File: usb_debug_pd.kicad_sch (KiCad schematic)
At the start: 87 parts, among them J4 Tag-Connect_TC2050-IDC-NL_2x5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, J7 USB-C_Kycon_KUSBX-SL2-CS1N24-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, Q12 DMG1012T-7, Q3 DMG1012T-7, U29 W25Q80DV_USON, U30 TPS65988DHRSHR, U31 NTS0102_XSON, U32 NCP718BSN330T1G, U34 FT230X_QFN, U40 AP22615A_TSOT26, U42 TPD4E05U06QDQARQ1

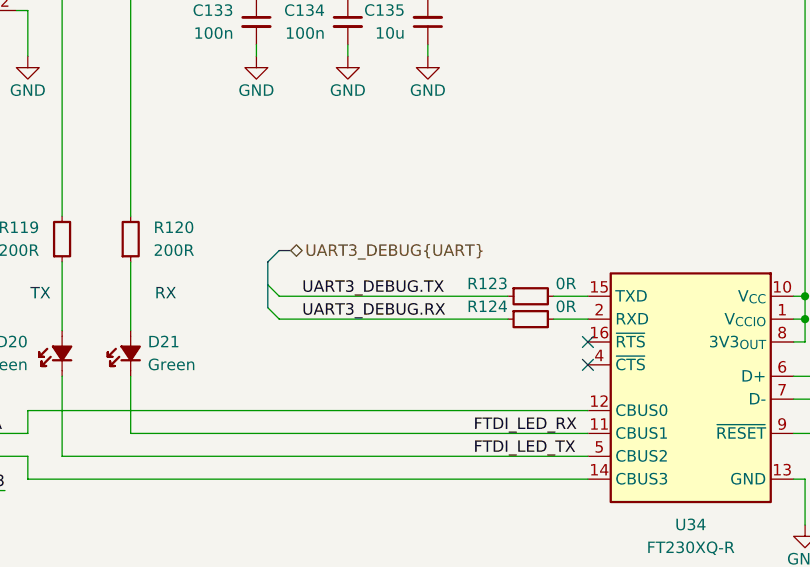
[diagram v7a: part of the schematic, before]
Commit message: [#85326] Update level shifters, fix UART cross
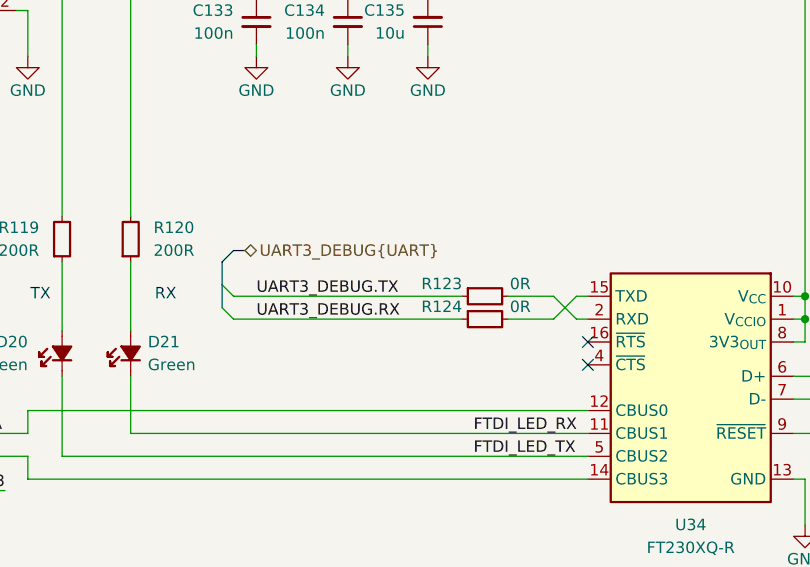
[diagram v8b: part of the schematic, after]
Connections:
- net at R124.2: now also U34.15 (TXD); no longer U34.2 (RXD)
- net at R123.2: now also U34.2 (RXD); no longer U34.15 (TXD)
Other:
- moved on the sheet: R123, R124
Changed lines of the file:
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@@
 	)
 	(bus_entry
-		(at 135.89 100.33)
+		(at 130.81 100.33)
 		(size 1.27 1.27)
 		(stroke
@@
 	)
 	(bus_entry
-		(at 135.89 97.79)
+		(at 130.81 97.79)
 		(size 1.27 1.27)
 		(stroke
@@
 	(wire
 		(pts
+			(xy 162.56 99.06) (xy 167.64 99.06)
+		)
+		(stroke
+			(width 0)
+			(type default)
+		)
+	)
+	(wire
+		(pts
 			(xy 227.33 114.3) (xy 212.09 114.3)
 		)
@@
 	(wire
 		(pts
+			(xy 170.18 101.6) (xy 167.64 99.06)
+		)
+		(stroke
+			(width 0)
+			(type default)
+		)
+	)
+	(wire
+		(pts
 			(xy 330.2 201.93) (xy 328.93 201.93)
 		)
@@
 	(bus
 		(pts
-			(xy 137.16 93.98) (xy 135.89 95.25)
+			(xy 132.08 93.98) (xy 130.81 95.25)
 		)
 		(stroke
@@
 	(wire
 		(pts
-			(xy 171.45 99.06) (xy 167.64 99.06)
-		)
-		(stroke
-			(width 0)
-			(type default)
-		)
-	)
-	(wire
-		(pts
 			(xy 140.97 215.9) (xy 149.86 215.9)
 		)
@@
 	(wire
 		(pts
-			(xy 171.45 101.6) (xy 167.64 101.6)
+			(xy 217.17 257.81) (xy 242.57 257.81)
 		)
 		(stroke
@@
 	(wire
 		(pts
-			(xy 217.17 257.81) (xy 242.57 257.81)
+			(xy 162.56 101.6) (xy 167.64 101.6)
 		)
 		(stroke
@@
 	(wire
 		(pts
+			(xy 170.18 99.06) (xy 171.45 99.06)
+		)
+		(stroke
+			(width 0)
+			(type default)
+		)
+	)
+	(wire
+		(pts
 			(xy 245.11 222.25) (xy 245.11 217.17)
 		)
@@
 		)
 	)
+	(wire
+		(pts
+			(xy 170.18 101.6) (xy 171.45 101.6)
+		)
+		(stroke
+			(width 0)
+			(type default)
+		)
+	)
 	(bus
 		(pts
-			(xy 135.89 95.25) (xy 135.89 97.79)
+			(xy 130.81 95.25) (xy 130.81 97.79)
 		)
 		(stroke
@@
 	(bus
 		(pts
-			(xy 138.43 93.98) (xy 137.16 93.98)
+			(xy 133.35 93.98) (xy 132.08 93.98)
 		)
 		(stroke
@@
 	(bus
 		(pts
-			(xy 135.89 97.79) (xy 135.89 100.33)
+			(xy 130.81 97.79) (xy 130.81 100.33)
 		)
 		(stroke
@@
 	(wire
 		(pts
-			(xy 137.16 101.6) (xy 162.56 101.6)
+			(xy 132.08 101.6) (xy 157.48 101.6)
 		)
 		(stroke
@@
 	(wire
 		(pts
-			(xy 137.16 99.06) (xy 162.56 99.06)
+			(xy 170.18 99.06) (xy 167.64 101.6)
+		)
+		(stroke
+			(width 0)
+			(type default)
+		)
+	)
+	(wire
+		(pts
+			(xy 132.08 99.06) (xy 157.48 99.06)
 		)
 		(stroke
@@
 	)
 	(label "UART3_DEBUG.RX"
-		(at 139.7 101.6 0)
+		(at 134.62 101.6 0)
 		(effects
 			(font
@@
 	)
 	(label "UART3_DEBUG.TX"
-		(at 139.7 99.06 0)
+		(at 134.62 99.06 0)
 		(effects
 			(font
@@
 	(hierarchical_label "UART3_DEBUG{UART}"
 		(shape bidirectional)
-		(at 138.43 93.98 0)
+		(at 133.35 93.98 0)
 		(effects
 			(font
@@
 	(symbol
 		(lib_id "antmicroResistors0402:R_0R_0402")
-		(at 162.56 101.6 0)
+		(at 157.48 101.6 0)
 		(unit 1)
 		(exclude_from_sim no)
@@
 		(dnp no)
 		(property "Reference" "R124"
-			(at 162.56 100.965 0)
+			(at 157.48 100.965 0)
 			(effects
 				(font
@@
 		)
 		(property "Value" "R_0R_0402"
-			(at 182.88 114.3 0)
+			(at 177.8 114.3 0)
 			(effects
 				(font
@@
 		)
 		(property "Footprint" "antmicro-footprints:R_0402_1005Metric"
-			(at 182.88 116.84 0)
+			(at 177.8 116.84 0)
 			(effects
 				(font
@@
 		)
 		(property "Datasheet" "https://industrial.panasonic.com/cdbs/www-data/pdf/RDA0000/AOA0000C301.pdf"
-			(at 182.88 119.38 0)
+			(at 177.8 119.38 0)
 			(effects
 				(font
@@
 		)
 		(property "Description" "SMD Chip Resistor, Jumper, 0 ohm, 100 mW, 0402 [1005 Metric], Thick Film, General Purpose"
-			(at 162.56 101.6 0)
+			(at 157.48 101.6 0)
 			(effects
 				(font
@@
 		)
 		(property "Manufacturer" "Panasonic"
-			(at 182.88 124.46 0)
+			(at 177.8 124.46 0)
 			(effects
 				(font
@@
 		)
 		(property "MPN" "ERJ2GE0R00X"
-			(at 182.88 121.92 0)
+			(at 177.8 121.92 0)
 			(effects
 				(font
@@
 		)
 		(property "Val" "0R"
-			(at 170.18 100.965 0)
+			(at 165.1 100.965 0)
 			(effects
 				(font
@@
 		)
 		(property "License" "Apache-2.0"
-			(at 182.88 127 0)
+			(at 177.8 127 0)
 			(effects
 				(font
@@
 		)
 		(property "Author" "Antmicro"
-			(at 182.88 129.54 0)
+			(at 177.8 129.54 0)
 			(effects
 				(font
@@
 		)
 		(property "Tolerance" "~"
-			(at 182.88 111.76 0)
+			(at 177.8 111.76 0)
 			(effects
 				(font
@@
 		)
 		(property "Current" "1A"
-			(at 182.88 132.08 0)
+			(at 177.8 132.08 0)
 			(effects
 				(font
@@
 	(symbol
 		(lib_id "antmicroResistors0402:R_0R_0402")
-		(at 162.56 99.06 0)
+		(at 157.48 99.06 0)
 		(unit 1)
 		(exclude_from_sim no)
@@
 		(dnp no)
 		(property "Reference" "R123"
-			(at 162.56 98.425 0)
+			(at 157.48 98.425 0)
 			(effects
 				(font
@@
 		)
 		(property "Value" "R_0R_0402"
-			(at 182.88 111.76 0)
+			(at 177.8 111.76 0)
 			(effects
 				(font
@@
 		)
 		(property "Footprint" "antmicro-footprints:R_0402_1005Metric"
-			(at 182.88 114.3 0)
+			(at 177.8 114.3 0)
 			(effects
 				(font
@@
 		)
 		(property "Datasheet" "https://industrial.panasonic.com/cdbs/www-data/pdf/RDA0000/AOA0000C301.pdf"
-			(at 182.88 116.84 0)
+			(at 177.8 116.84 0)
 			(effects
 				(font
@@
 		)
 		(property "Description" "SMD Chip Resistor, Jumper, 0 ohm, 100 mW, 0402 [1005 Metric], Thick Film, General Purpose"
-			(at 162.56 99.06 0)
+			(at 157.48 99.06 0)
 			(effects
 				(font
@@
 		)
 		(property "Manufacturer" "Panasonic"
-			(at 182.88 121.92 0)
+			(at 177.8 121.92 0)
 			(effects
 				(font
@@
 		)
 		(property "MPN" "ERJ2GE0R00X"
-			(at 182.88 119.38 0)
+			(at 177.8 119.38 0)
 			(effects
 				(font
@@
 		)
 		(property "Val" "0R"
-			(at 170.18 98.425 0)
+			(at 165.1 98.425 0)
 			(effects
 				(font
@@
 		)
 		(property "License" "Apache-2.0"
-			(at 182.88 124.46 0)
+			(at 177.8 124.46 0)
 			(effects
 				(font
@@
 		)
 		(property "Author" "Antmicro"
-			(at 182.88 127 0)
+			(at 177.8 127 0)
 			(effects
 				(font
@@
 		)
 		(property "Tolerance" "~"
-			(at 182.88 109.22 0)
+			(at 177.8 109.22 0)
 			(effects
 				(font
@@
 		)
 		(property "Current" "1A"
-			(at 182.88 129.54 0)
+			(at 177.8 129.54 0)
 			(effects
 				(font
